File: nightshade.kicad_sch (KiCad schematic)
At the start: 80 parts, among them J1 Bus_ISA_16bit, J2 DE15_Plug_HighDensity_Mountin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, U1 GD542x_ISA, U2 SOJ_256Kx16, U3 SOJ_256Kx16, U4 LM334M, U5 LDK320AM50R, U6 27C256, U7 74LS244, Y1 14.31818MHz

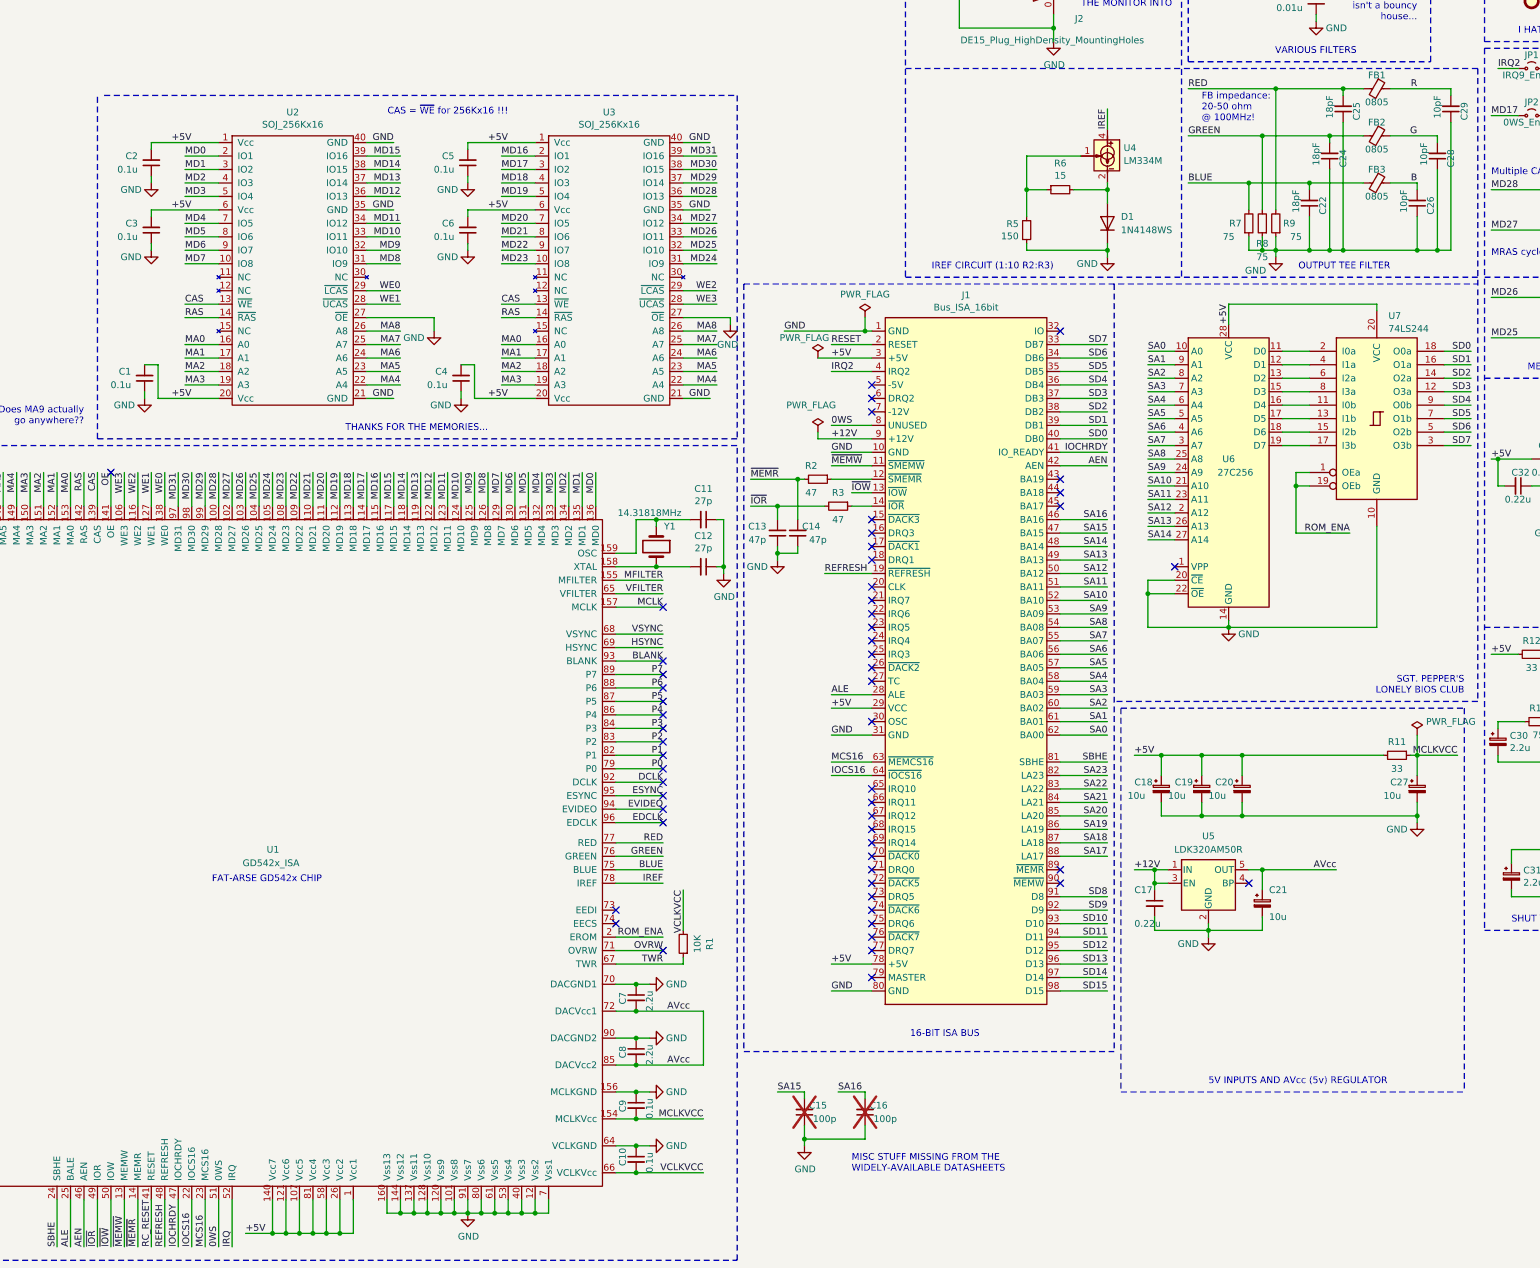
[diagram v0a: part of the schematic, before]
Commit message: Add files via upload
Updated with corrected parts lists etc.
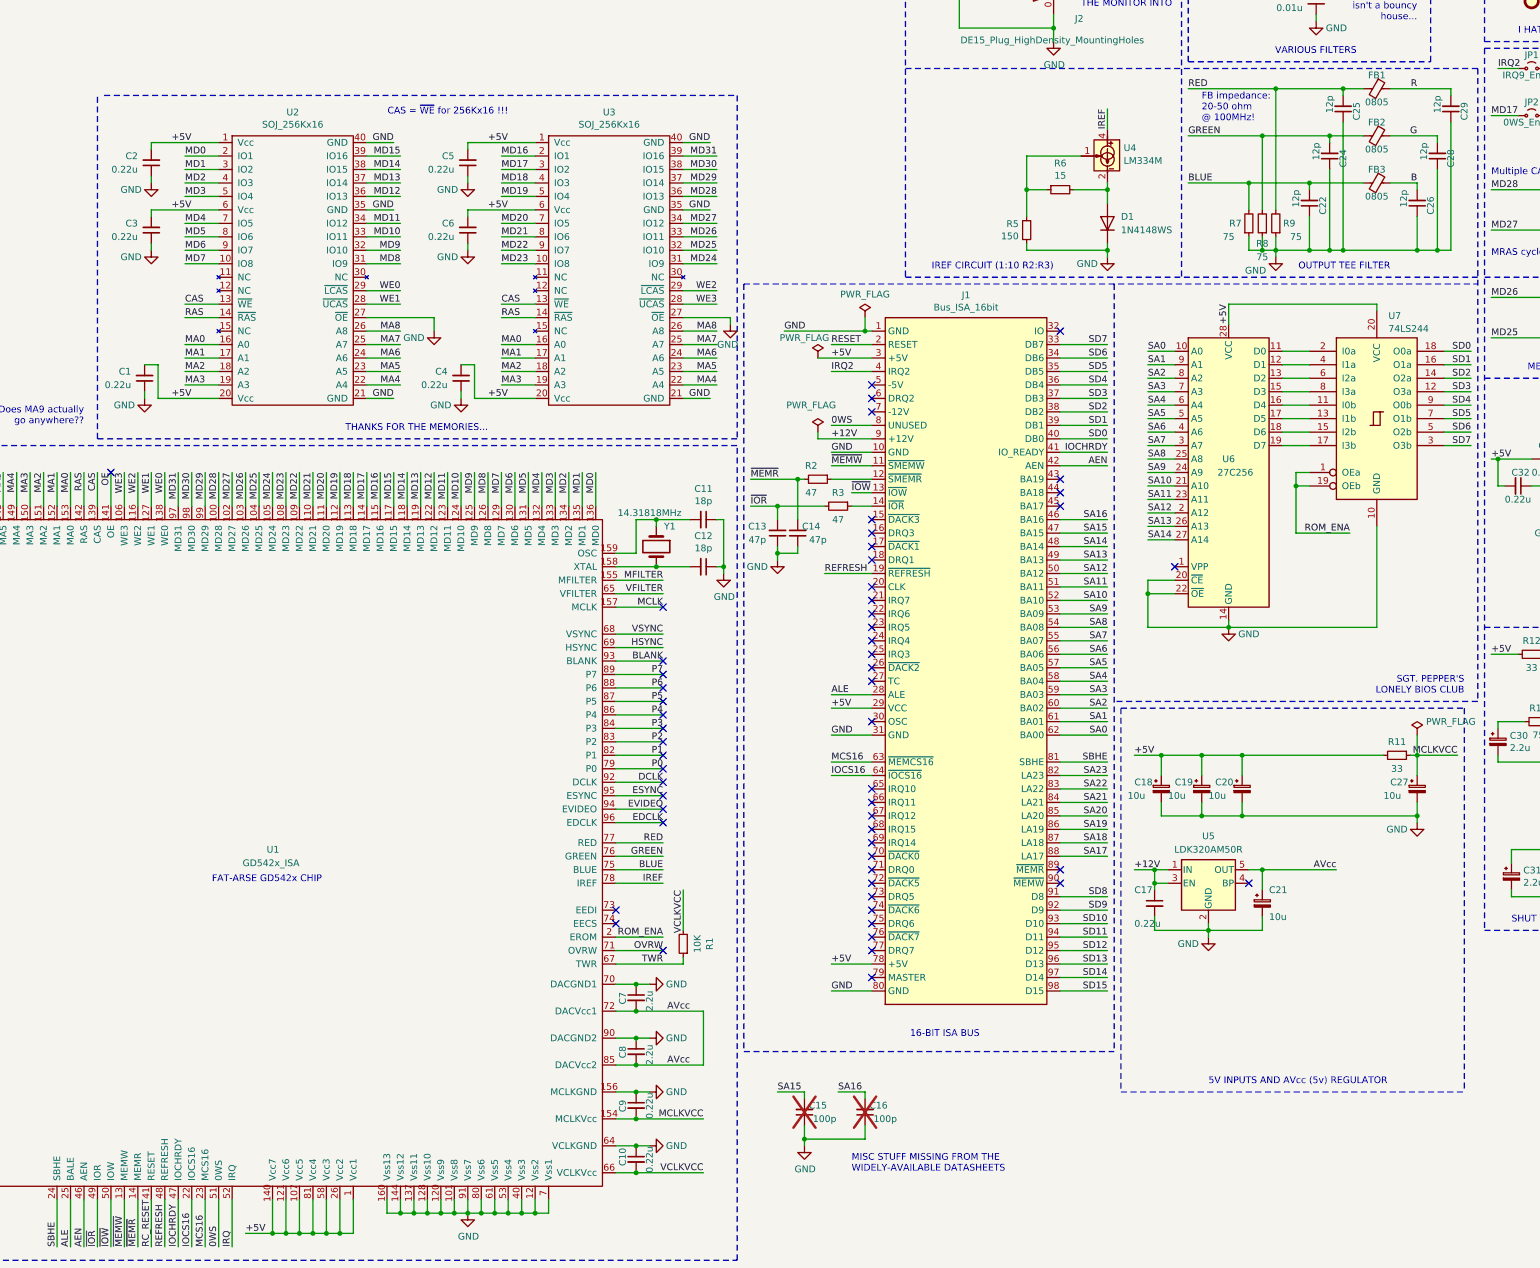
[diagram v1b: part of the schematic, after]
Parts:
- C1, C10, C2, C3, C4, C5, C6, C9: value 0.1u -> 0.22u
- C11, C12: value 27p -> 18p
- C22, C24, C25: value 18pF -> 12p
- C26, C28, C29: value 10pF -> 12p
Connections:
- new net: U4.3, U4.5 (NC)
- new net: U4.6, U4.7, U4.8 (NC)
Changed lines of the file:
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@@
 			)
 		)
-		(property "Value" "0.1u"
+		(property "Value" "0.22u"
 			(at 210.82 266.7 90)
 			(effects
@@
 			)
 		)
-		(property "Value" "0.1u"
+		(property "Value" "0.22u"
 			(at 210.82 256.54 90)
 			(effects
@@
 			)
 		)
-		(property "Value" "27p"
+		(property "Value" "18p"
 			(at 220.98 140.0048 90)
 			(effects
@@
 			)
 		)
-		(property "Value" "27p"
+		(property "Value" "18p"
 			(at 220.98 148.8948 90)
 			(effects
@@
 			)
 		)
-		(property "Value" "18pF"
+		(property "Value" "12p"
 			(at 339.09 63.5 90)
 			(effects
@@
 			)
 		)
-		(property "Value" "18pF"
+		(property "Value" "12p"
 			(at 336.55 72.39 90)
 			(effects
@@
 			)
 		)
-		(property "Value" "18pF"
+		(property "Value" "12p"
 			(at 332.74 81.28 90)
 			(effects
@@
 			)
 		)
-		(property "Value" "10pF"
+		(property "Value" "12p"
 			(at 353.06 81.28 90)
 			(effects
@@
 			)
 		)
-		(property "Value" "10pF"
+		(property "Value" "12p"
 			(at 356.87 72.39 90)
 			(effects
@@
 			)
 		)
-		(property "Value" "10pF"
+		(property "Value" "12p"
 			(at 359.41 63.5 90)
 			(effects
@@
 			)
 		)
-		(property "Value" "0.1u"
+		(property "Value" "0.22u"
 			(at 114.3 90.17 0)
 			(effects
@@
 			)
 		)
-		(property "Value" "0.1u"
+		(property "Value" "0.22u"
 			(at 114.3 77.47 0)
 			(effects
@@
 			)
 		)
-		(property "Value" "0.1u"
+		(property "Value" "0.22u"
 			(at 113.03 118.11 0)
 			(effects
@@
 			)
 		)
-		(property "Value" "0.1u"
+		(property "Value" "0.22u"
 			(at 173.99 90.17 0)
 			(effects
@@
 			)
 		)
-		(property "Value" "0.1u"
+		(property "Value" "0.22u"
 			(at 173.99 77.47 0)
 			(effects
@@
 			)
 		)
-		(property "Value" "0.1u"
+		(property "Value" "0.22u"
 			(at 172.72 118.11 0)
 			(effects
@@
 		(pin "6"
 		)
+		(pin "6"
+		)
+		(pin "8"
+		)
+		(pin "5"
+		)
+		(pin "7"
+		)
+		(pin "3"
+		)
 		(instances

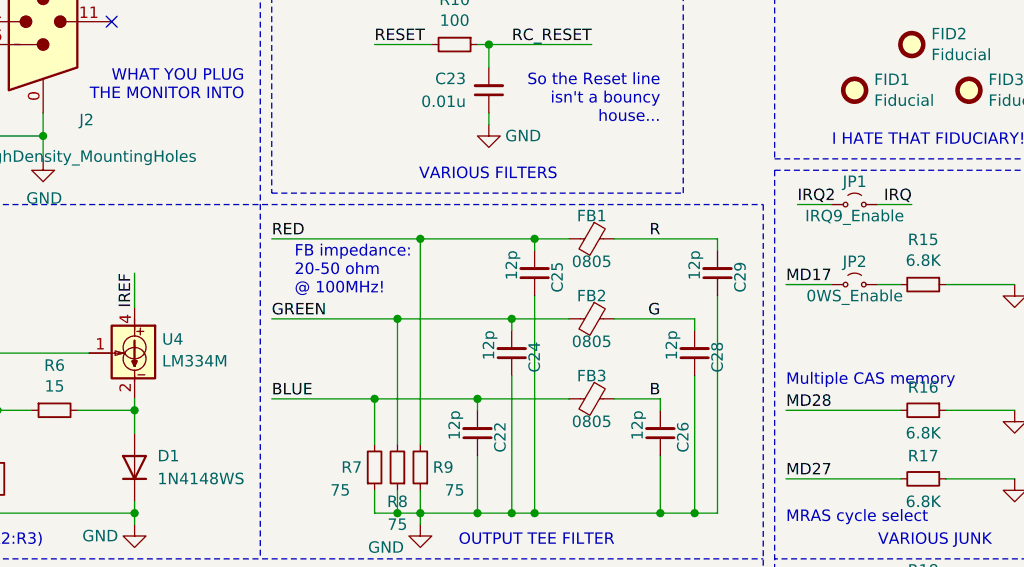
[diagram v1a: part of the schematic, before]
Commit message: Add files via upload
Updated to KiCAD 9.x, fixed some bugs in the silkscreening
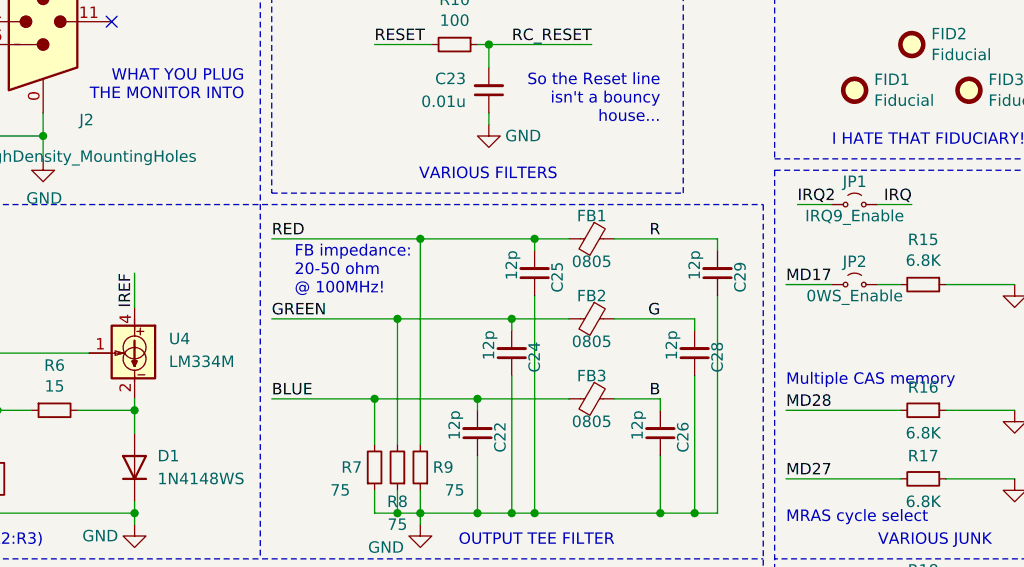
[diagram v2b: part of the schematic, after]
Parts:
- J2: symbol Connector:DE15_Plug_HighDensity_MountingHoles -> Connector:DE15_Pins_HighDensity_MountingHoles
- U4: footprint PDVGA:SOIC-8_DMP-8 -> Package_SO:SOIC-8_3.9x4.9mm_P1.27mm

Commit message: Add files via upload
Updated to Cherry Tomato V1.0 revision
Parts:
- removed C15, C16: 100p, Capacitor_SMD:C_0805_2012Metric, symbol Device:C_Small
- removed C21: 10u, Capacitor_SMD:C_1206_3216Metric, symbol Device:C_Polarized_Small
- removed C3, C6: 0.22u, Capacitor_SMD:C_0805_2012Metric, symbol Device:C_Small
- removed D1: 1N4148WS, Diode_SMD:D_SOD-323_HandSoldering, symbol Diode:1N4148WS
- removed FB1, FB2, FB3: 0805, Inductor_SMD:L_0805_2012Metric, symbol Device:FerriteBead_Small
- removed U4: LM334M, Package_SO:SOIC-8_3.9x4.9mm_P1.27mm, symbol Reference_Current:LM334M
- removed U5: LDK320AM50R, Package_TO_SOT_SMD:SOT-23-5_HandSoldering, symbol Regulator_Linear:LDK130-33_SOT23_SOT353
- removed U7: 74LS244, Package_SO:SSOP-20_5.3x7.2mm_P0.65mm, symbol 74xx:74LS244
- added C15, C43: 10u, Capacitor_SMD:C_1206_3216Metric, symbol Device:C_Polarized_Small
- added C16: 4.7u, Capacitor_SMD:CP_Elec_3x5.4, symbol Device:C_Polarized_Small
- added F1: 0805L020YR, Fuse:Fuse_0805_2012Metric, symbol Device:Polyfuse_Small
- added J3: Conn_02x13_Odd_Even, Connector_PinHeader_2.54mm:PinHeader_2x13_P2.54mm_Vertical, symbol Connector_Generic:Conn_02x13_Odd_Even
- added JP3: 16bit_BIOS, Connector_PinHeader_2.54mm:PinHeader_1x02_P2.54mm_Vertical, symbol Jumper:Jumper_2_Small_Open
- added L1, L2, L3: 1210, Inductor_SMD:L_1206_3216Metric, symbol Device:L_Small
- added Q1: MMBT3904, Package_TO_SOT_SMD:SOT-23, symbol Transistor_BJT:MMBT3904
- added R20: 33, Resistor_SMD:R_0603_1608Metric, symbol Device:R_Small
- added R21: 6.8K, Resistor_SMD:R_0805_2012Metric, symbol Device:R_Small
- added R22: 33, Resistor_SMD:R_0805_2012Metric, symbol Device:R_Small
- added R23, R24: 1K, Resistor_SMD:R_0603_1608Metric, symbol Device:R_Small
- added R25, R26: 16, Resistor_SMD:R_0603_1608Metric, symbol Device:R_Small
- added U10, U8: 74HCT244, PDVGA:SSOP-20_4.4_5.3x6.5mm_P0.65mm, symbol 74xx:74HCT244
- added U12: L78L05_TO92, Package_TO_SOT_THT:TO-92_Inline, symbol Regulator_Linear:L78L05_TO92
- added U4: TL431DBZ, Package_TO_SOT_SMD:SOT-23, symbol Reference_Voltage:TL431DBZ
- added U5: 93CxxA, PDVGA:SOIC-8_DMP-8, symbol Memory_EEPROM:93CxxC
- added U9: 27C256, Package_DIP:DIP-28_W15.24mm_Socket, symbol Memory_EPROM:27C256
- C1, C10, C17, C2, C32, C33, C34, C35, C36, C37, C38, C39, C4, C40, C41, C42, C5, C9: value 0.22u -> 0.1u
- C22, C24, C25: value 12p -> 0.1u
- C26, C28, C29: value 12p -> 47pF; footprint Capacitor_SMD:C_0805_2012Metric -> Capacitor_SMD:C_0603_1608Metric
- C7, C8: value 2.2u -> 10u
- JP2: footprint Resistor_SMD:R_0805_2012Metric -> Connector_PinHeader_2.54mm:PinHeader_1x02_P2.54mm_Vertical
- R11, R12, R7, R8, R9: footprint Resistor_SMD:R_0805_2012Metric -> Resistor_SMD:R_0603_1608Metric
- R2: value 47 -> 33; footprint Resistor_SMD:R_0805_2012Metric -> Resistor_SMD:R_0603_1608Metric; now not fitted
- R4: value EhWot -> 33; footprint Resistor_SMD:R_0805_2012Metric -> Resistor_SMD:R_0603_1608Metric
- R5: value 150 -> 1K
- R6: value 15 -> 270-300
- U1, U2, U3: now not fitted
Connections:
- net +12V: now also C15.1, U12.3 (VI)
- net +5V: now also C22.2, C24.2, C25.2, R1.2, U6.1 (VPP), C43.1, F1.1, U10.20 (VCC), U5.6 (ORG), U5.8 (VCC), U8.20 (VCC), U9.1 (VPP), U9.10 (A0), U9.28 (VCC)
- net AVcc: now also R5.1, C16.1, U12.1 (VO)
- net B: now also L3.2
- net BLANK: now also J3.20 (Pin_20)
- net BLUE: now also L3.1; no longer C22.2
- net DCLK: now also R2.1
- net EDCLK: now also J3.11 (Pin_11)
- net ESYNC: now also R24.2, U5.2 (SCLK)
- net EVIDEO: now also R23.2, U5.3 (DI)
- net G: now also L2.2
- net GND: now also J2.10, R6.2, C15.2, C16.2, C43.2, J3.1 (Pin_1), J3.15 (Pin_15), J3.17 (Pin_17), J3.19 (Pin_19), J3.21 (Pin_21), J3.23 (Pin_23), J3.26 (Pin_26), J3.3 (Pin_3), J3.5 (Pin_5), R21.1, U10.10 (GND), U12.2 (GND), U4.3 (A), U5.5 (GND), U8.10 (GND), U9.14 (GND), U9.20 (~{CE}), U9.22 (~{OE}); no longer R4.2, R5.1
- net GREEN: now also L2.1; no longer C24.2
- net HSYNC: now also R4.1, R26.2; no longer J2.13
- net IREF: now also Q1.3 (C)
- net MD22: now also JP3.1 (A)
- net P0: now also J3.2 (Pin_2)
- net P1: now also J3.4 (Pin_4)
- net P2: now also J3.6 (Pin_6)
- net P3: now also J3.8 (Pin_8)
- net P4: now also J3.10 (Pin_10)
- net P5: now also J3.12 (Pin_12)
- net P6: now also J3.14 (Pin_14)
- net P7: now also J3.16 (Pin_16)
- net R: now also L1.2
- net RED: now also L1.1; no longer C25.2
- net ROM_ENA: now also U10.1 (1OE), U10.19 (2OE), U8.1 (1OE), U8.19 (2OE)
- net SA1: now also U9.9 (A1)
- net SA10: now also U9.21 (A10)
- net SA11: now also U9.23 (A11)
- net SA12: now also U9.2 (A12)
- net SA13: now also U9.26 (A13)
- net SA14: now also U9.27 (A14)
- net SA2: now also U9.8 (A2)
- net SA3: now also U9.7 (A3)
- net SA4: now also U9.6 (A4)
- net SA5: now also U9.5 (A5)
- net SA6: now also U9.4 (A6)
- net SA7: now also U9.3 (A7)
- net SA8: now also U9.25 (A8)
- net SA9: now also U9.24 (A9)
- net SD0: now also U8.3 (2Y0)
- net SD1: now also U8.5 (2Y1)
- net SD10: now also U10.16 (1Y1)
- net SD11: now also U10.18 (1Y0)
- net SD12: now also U10.9 (2Y3)
- net SD13: now also U10.7 (2Y2)
- net SD14: now also U10.5 (2Y1)
- net SD15: now also U10.3 (2Y0)
- net SD2: now also U8.7 (2Y2)
- net SD3: now also U8.9 (2Y3)
- net SD4: now also U8.18 (1Y0)
- net SD5: now also U8.16 (1Y1)
- net SD6: now also U8.14 (1Y2)
- net SD7: now also U8.12 (1Y3)
- net SD8: now also U10.12 (1Y3)
- net SD9: now also U10.14 (1Y2)
- net VCLKVCC: no longer R1.2
- net VSYNC: now also R20.1, R25.2; no longer J2.14
- net ~{MEMR}: now also R22.2; no longer R2.2
- net ~{SMEMR}: now reaches J1.12 (~{SMEMR})
- net ~{SMEMR}: now also R22.1; no longer R2.1
- net EEDI: now reaches U1.73 (EEDI)
- net EEDI: now also U5.4 (DO)
- net EECS: now reaches U1.74 (EECS)
- net EECS: now also U5.1 (CS)
- net D0: now reaches U6.11 (D0)
- net D0: now also U8.17 (2A0)
- net D1: now reaches U6.12 (D1)
- net D1: now also U8.15 (2A1)
- net D2: now reaches U6.13 (D2)
- net D2: now also U8.13 (2A2)
- net D3: now reaches U6.15 (D3)
- net D3: now also U8.11 (2A3)
- net D4: now reaches U6.16 (D4)
- net D4: now also U8.2 (1A0)
- net D5: now reaches U6.17 (D5)
- net D5: now also U8.4 (1A1)
- net D6: now reaches U6.18 (D6)
- net D6: now also U8.6 (1A2)
- net D7: now reaches U6.19 (D7)
- net D7: now also U8.8 (1A3)
- net at R6.1: now also Q1.2 (E), U4.2 (REF); no longer R5.2
- net at J2.9: now also F1.2
- net ~{MEMW} renamed ~{SMEMW}
- new net: Q1.1 (B), R5.2, U4.1 (K)
- new net: J3.18 (Pin_18), R2.2
- new net: J3.7 (Pin_7), R23.1
- new net: J3.9 (Pin_9), R24.1
- new net: JP3.2 (B), R21.2
- new net D10: U10.4 (1A1), U9.13 (D2)
- new net D11: U10.2 (1A0), U9.15 (D3)
- new net D12: U10.11 (2A3), U9.16 (D4)
- new net D13: U10.13 (2A2), U9.17 (D5)
- new net D14: U10.15 (2A1), U9.18 (D6)
- new net D15: U10.17 (2A0), U9.19 (D7)
- new net D8: U10.8 (1A3), U9.11 (D0)
- new net D9: U10.6 (1A2), U9.12 (D1)
- new net FHSYNC: J3.22 (Pin_22), R4.2
- new net FVSYNC: J3.24 (Pin_24), R20.2
- new net VHSYNC: J2.13, R26.1
- new net VVSYNC: J2.14, R25.1
- no-connect marks 62 -> 45
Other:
- note added: "16-bit BIOS"
- note added: "1ST MEG"
- note added: "IREF CIRCUIT (3:1 R5:R6)"
- note added: "IT'S A STORY... OF AN UGLY BIOS... MADE OF FOUR VERY, VERY UGLY CHIPS..."
- note added: "Inductor Z: 0.22 ohm"
- note added: "OH SEE THE SEEPROM..."
- note added: "OUTPUT FILTER"
- note added: "WORSE THAN USELESS FEATURE CONNECTOR"
- note removed: "FB impedance: 20-50 ohm @ 100MHz!"
- note removed: "IREF CIRCUIT (1:10 R2:R3)"
- note removed: "MISC STUFF MISSING FROM THE WIDELY-AVAILABLE DATASHEETS"
- note removed: "OUTPUT TEE FILTER"
- note removed: "SGT. PEPPER'S LONELY BIOS CLUB"
- moved on the sheet: C1, C13, C14, C17, C19, C2, C20, C23, C26, C27, C28, C29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
